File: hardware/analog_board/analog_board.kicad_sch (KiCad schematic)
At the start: 0 parts

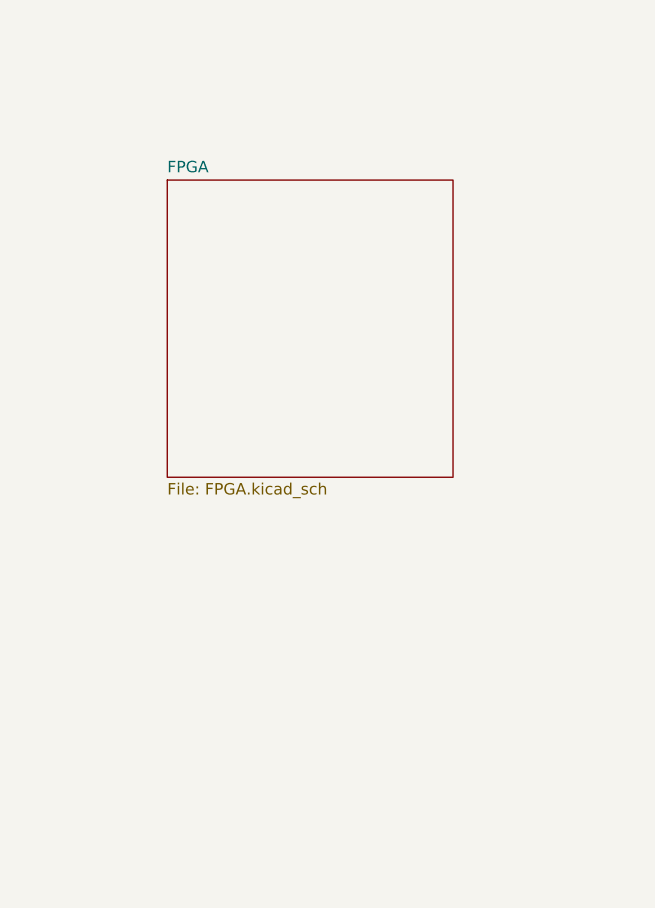
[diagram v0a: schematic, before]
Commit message: 1、FPGA最小系统原理图 2、DAC电路原理图 3、FPGA DAC 预布局
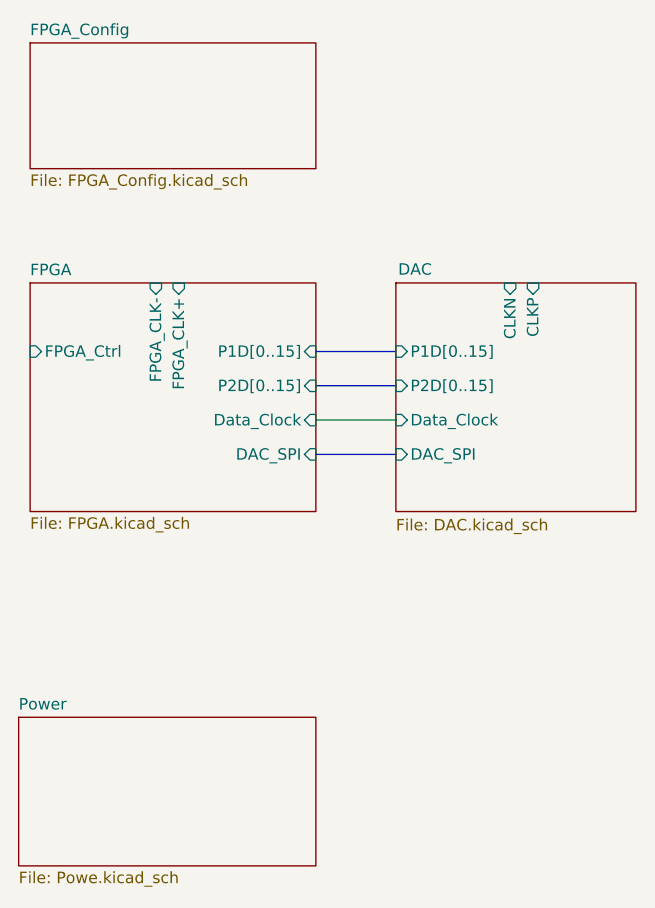
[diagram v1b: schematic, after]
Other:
- added sheet DAC (DAC.kicad_sch)
- added sheet FPGA_Config (FPGA_Config.kicad_sch)
- added sheet Power (Powe.kicad_sch)
- sheet FPGA ports: added DAC_SPI, Data_Clock, FPGA_CLK+, FPGA_CLK-, FPGA_Ctrl, P1D[0..15], P2D[0..15]; removed none

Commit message: feat：时钟电路原理图
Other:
- added sheet Clock (Clock.kicad_sch)
- sheet DAC ports: added DAC_CKL-, DAC_CLK+, OUT1, OUT2; removed CLKN, CLKP
- sheet FPGA ports: added Clock_NRST; removed none

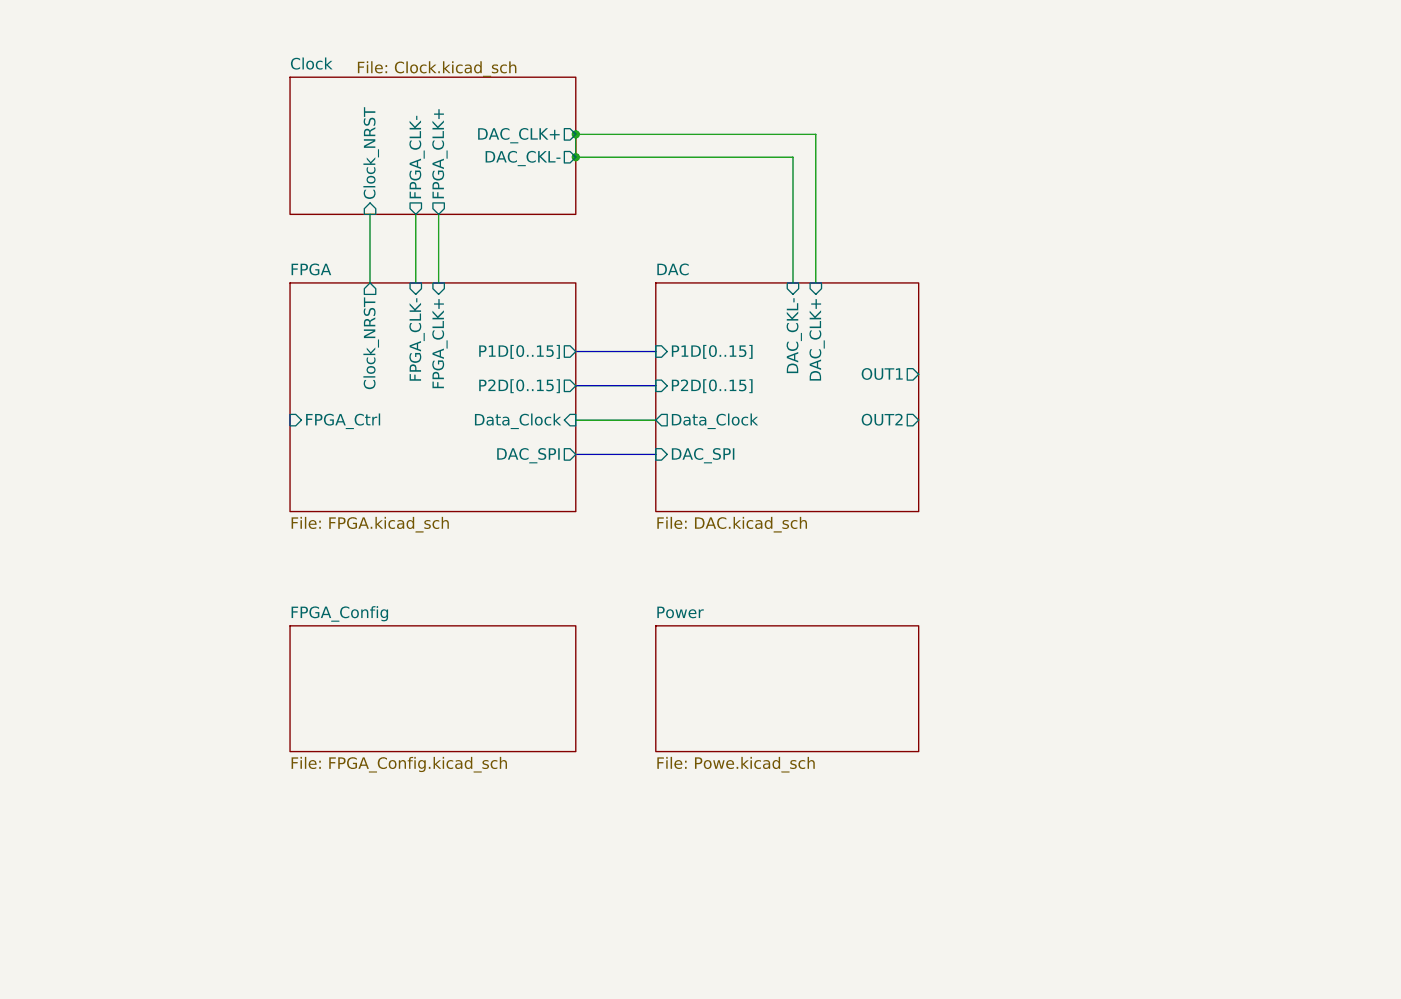
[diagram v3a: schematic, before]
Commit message: feat：完成模拟板板间接口设计
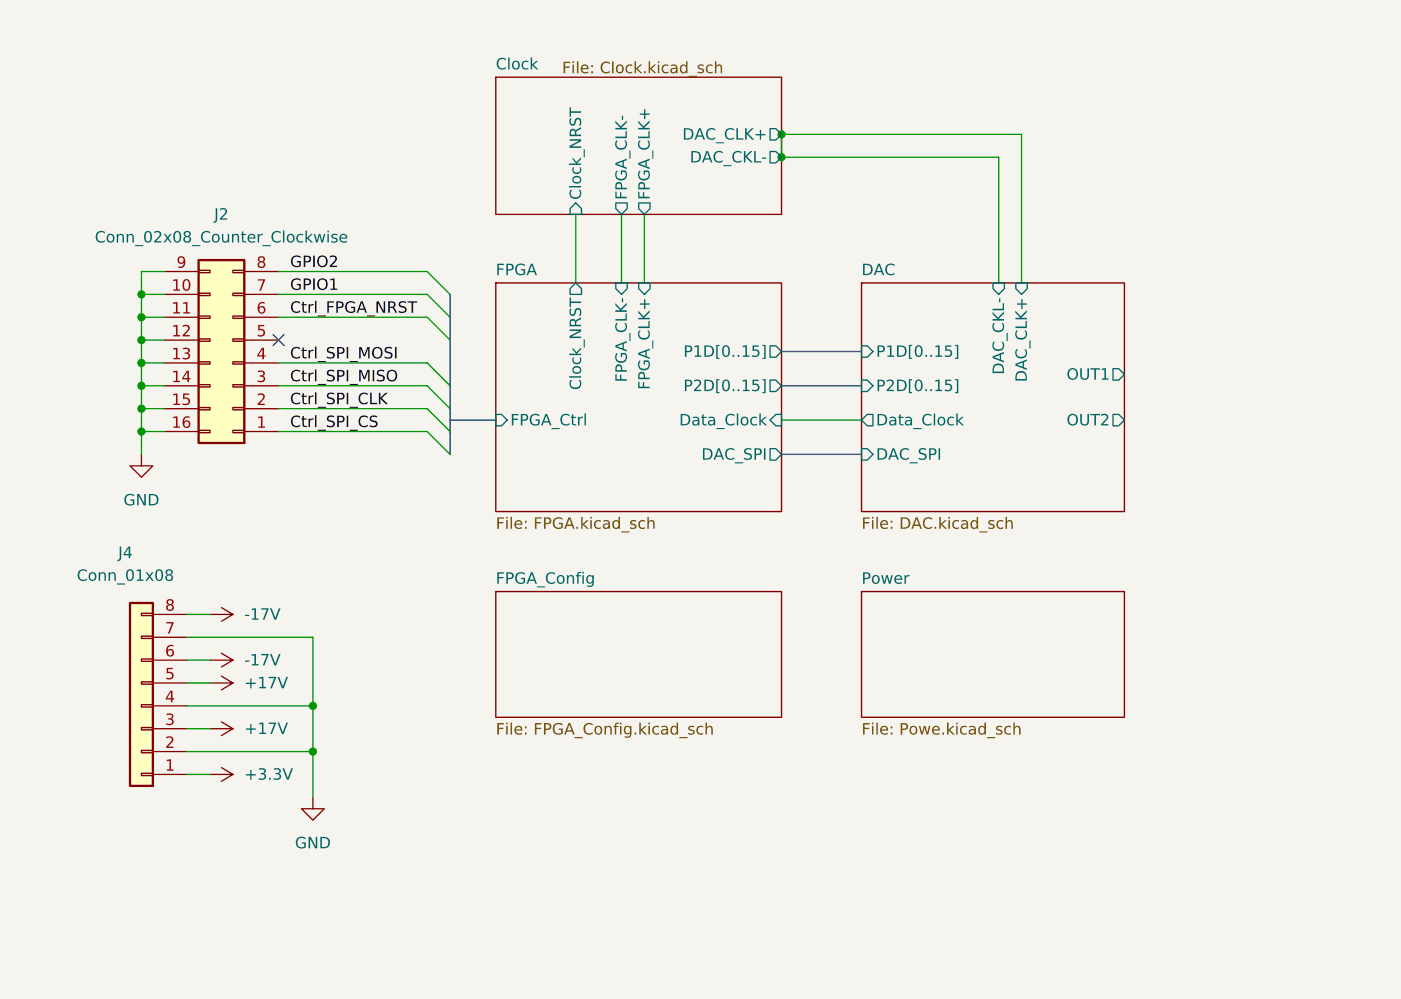
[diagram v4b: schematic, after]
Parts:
- added J2: Conn_02x08_Counter_Clockwise, Connector_IDC:IDC-Header_2x08_P2.54mm_Latch_Vertical, symbol Connector_Generic:Conn_02x08_Counter_Clockwise
- added J4: Conn_01x08, Connector_JST:JST_VH_B8P-VH-B_1x08_P3.96mm_Vertical, symbol Connector_Generic:Conn_01x08
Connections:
- new net +17V: J4.3 (Pin_3), J4.5 (Pin_5)
- new net +3.3V: J4.1 (Pin_1)
- new net -17V: J4.6 (Pin_6), J4.8 (Pin_8)
- new net Ctrl_FPGA_NRST: J2.6 (Pin_6)
- new net Ctrl_SPI_CLK: J2.2 (Pin_2)
- new net Ctrl_SPI_CS: J2.1 (Pin_1)
- new net Ctrl_SPI_MISO: J2.3 (Pin_3)
- new net Ctrl_SPI_MOSI: J2.4 (Pin_4)
- new net GND: J2.10 (Pin_10), J2.11 (Pin_11), J2.12 (Pin_12), J2.13 (Pin_13), J2.14 (Pin_14), J2.15 (Pin_15), J2.16 (Pin_16), J2.9 (Pin_9), J4.2 (Pin_2), J4.4 (Pin_4), J4.7 (Pin_7)
- new net GPIO1: J2.7 (Pin_7)
- new net GPIO2: J2.8 (Pin_8)
- no-connect marks 0 -> 1

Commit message: feat：模拟板电源 原理图设计
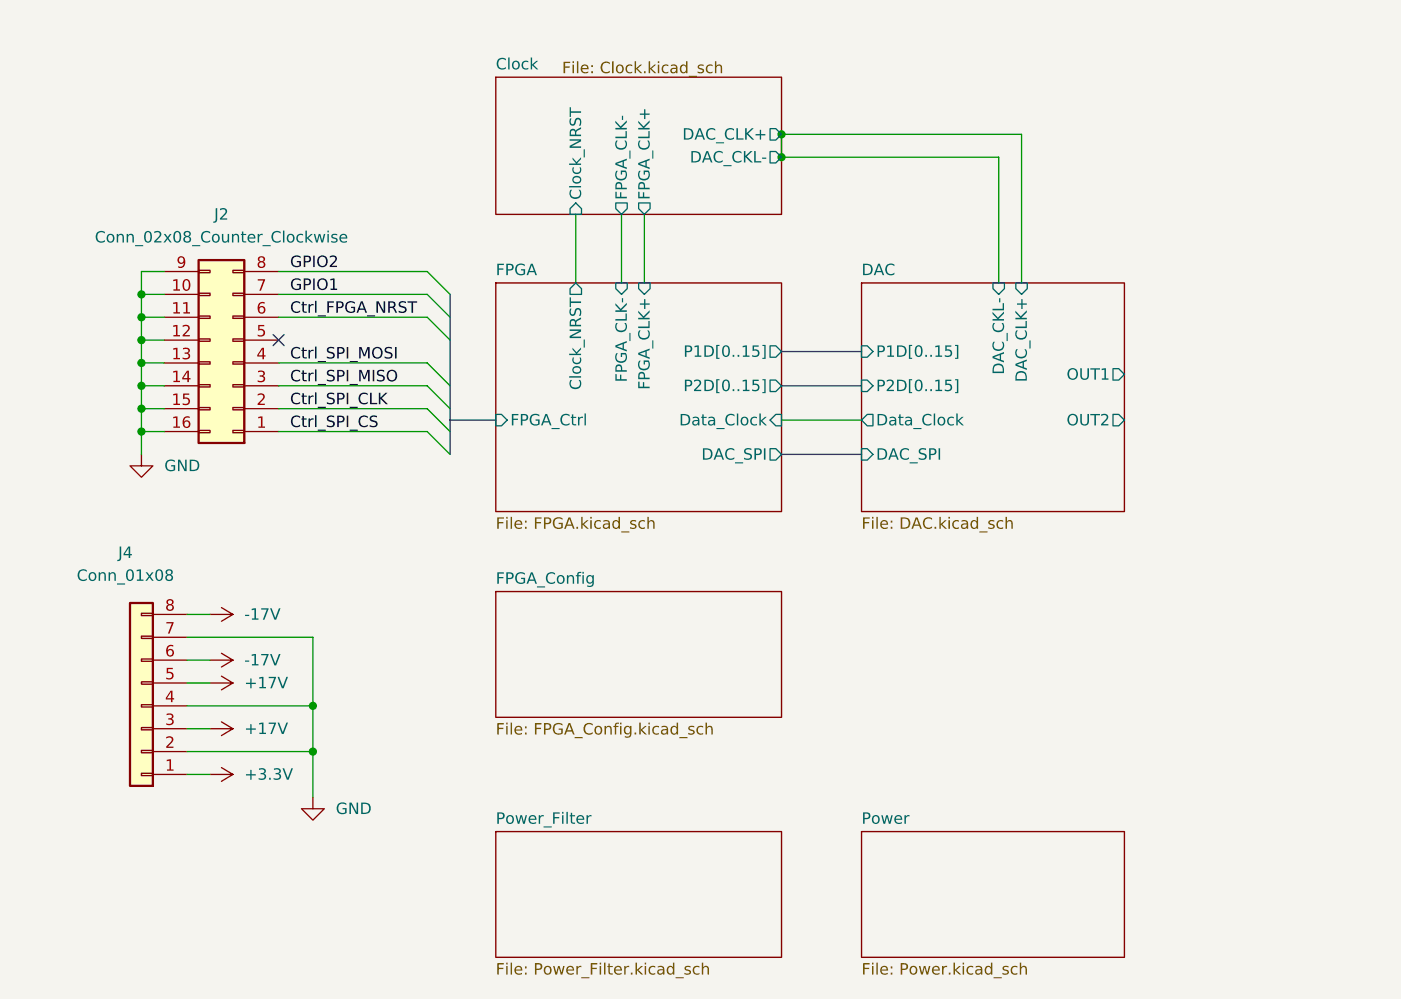
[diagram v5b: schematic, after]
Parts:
- J4: footprint Connector_JST:JST_VH_B8P-VH-B_1x08_P3.96mm_Vertical -> Connector_JST:JST_VH_B8P-VH_1x08_P3.96mm_Vertical
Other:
- added sheet Power_Filter (Power_Filter.kicad_sch)
- sheet Power: file Powe.kicad_sch -> Power.kicad_sch
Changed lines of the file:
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@@
 		)
 		(property "Value" "GND"
-			(at 43.18 129.54 0)
-			(show_name no)
-			(do_not_autoplace no)
-			(effects
-				(font
-					(size 1.27 1.27)
-				)
+			(at 45.72 125.7299 0)
+			(show_name no)
+			(do_not_autoplace no)
+			(effects
+				(font
+					(size 1.27 1.27)
+				)
+				(justify left)
 			)
 		)
@@
 		)
 		(property "Value" "GND"
-			(at 24.13 91.44 0)
-			(show_name no)
-			(do_not_autoplace no)
-			(effects
-				(font
-					(size 1.27 1.27)
-				)
+			(at 26.67 87.6299 0)
+			(show_name no)
+			(do_not_autoplace no)
+			(effects
+				(font
+					(size 1.27 1.27)
+				)
+				(justify left)
 			)
 		)
@@
 			)
 		)
-		(property "Footprint" "Connector_JST:JST_VH_B8P-VH-B_1x08_P3.96mm_Vertical"
+		(property "Footprint" "Connector_JST:JST_VH_B8P-VH_1x08_P3.96mm_Vertical"
 			(at 24.13 114.3 0)
 			(hide yes)
@@
 			(project "analog_board"
 				(path "/ca4be128-f2cd-4bef-b262-ed123f9c630d"
-					(page "5")
+					(page "4")
 				)
 			)
@@
 	)
 	(sheet
-		(at 63.5 44.45)
-		(size 31.75 15.24)
-		(exclude_from_sim no)
-		(in_bom yes)
-		(on_board yes)
-		(dnp no)
-		(stroke
-			(width 0.1524)
-			(type solid)
-		)
-		(fill
-			(color 0 0 0 0)
-		)
-		(property "Sheetname" "Clock"
-			(at 63.5 43.7384 0)
-			(show_name no)
-			(do_not_autoplace no)
-			(effects
-				(font
-					(size 1.27 1.27)
-				)
-				(justify left bottom)
-			)
-		)
-		(property "Sheetfile" "Clock.kicad_sch"
-			(at 70.866 42.672 0)
-			(show_name no)
-			(do_not_autoplace no)
-			(effects
-				(font
-					(size 1.27 1.27)
-				)
-				(justify left top)
-			)
-		)
-		(pin "FPGA_CLK+" output
-			(at 80.01 59.69 270)
-			(effects
-				(font
-					(size 1.27 1.27)
-				)
-				(justify left)
-			)
-		)
-		(pin "FPGA_CLK-" output
-			(at 77.47 59.69 270)
-			(effects
-				(font
-					(size 1.27 1.27)
-				)
-				(justify left)
-			)
-		)
-		(pin "DAC_CLK+" output
-			(at 95.25 50.8 0)
-			(effects
-				(font
-					(size 1.27 1.27)
-				)
-				(justify right)
-			)
-		)
-		(pin "DAC_CKL-" output
-			(at 95.25 53.34 0)
-			(effects
-				(font
-					(size 1.27 1.27)
-				)
-				(justify right)
-			)
-		)
-		(pin "Clock_NRST" input
-			(at 72.39 59.69 270)
-			(effects
-				(font
-					(size 1.27 1.27)
-				)
-				(justify left)
-			)
-		)
-		(instances
-			(project "analog_board"
-				(path "/ca4be128-f2cd-4bef-b262-ed123f9c630d"
-					(page "6")
-				)
-			)
-		)
-	)
-	(sheet
-		(at 104.14 101.6)
+		(at 104.14 128.27)
 		(size 29.21 13.97)
 		(exclude_from_sim no)
@@
 		)
 		(property "Sheetname" "Power"
-			(at 104.14 100.8884 0)
+			(at 104.14 127.5584 0)
 			(show_name no)
 			(do_not_autoplace no)
@@
 			)
 		)
-		(property "Sheetfile" "Powe.kicad_sch"
-			(at 104.14 116.1546 0)
+		(property "Sheetfile" "Power.kicad_sch"
+			(at 104.14 142.8246 0)
 			(show_name no)
 			(do_not_autoplace no)
@@
 			(project "analog_board"
 				(path "/ca4be128-f2cd-4bef-b262-ed123f9c630d"
-					(page "4")
-				)
-			)
+					(page "7")
+				)
+			)
+		)
+	)
+	(sheet
+		(at 63.5 44.45)
+		(size 31.75 15.24)
+		(exclude_from_sim no)
+		(in_bom yes)
+		(on_board yes)
+		(dnp no)
+		(stroke
+			(width 0.1524)
+			(type solid)
+		)
+		(fill
+			(color 0 0 0 0)
+		)
+		(property "Sheetname" "Clock"
+			(at 63.5 43.7384 0)
+			(show_name no)
+			(do_not_autoplace no)
+			(effects
+				(font
+					(size 1.27 1.27)
+				)
+				(justify left bottom)
+			)
+		)
+		(property "Sheetfile" "Clock.kicad_sch"
+			(at 70.866 42.672 0)
+			(show_name no)
+			(do_not_autoplace no)
+			(effects
+				(font
+					(size 1.27 1.27)
+				)
+				(justify left top)
+			)
+		)
+		(pin "FPGA_CLK+" output
+			(at 80.01 59.69 270)
+			(effects
+				(font
+					(size 1.27 1.27)
+				)
+				(justify left)
+			)
+		)
+		(pin "FPGA_CLK-" output
+			(at 77.47 59.69 270)
+			(effects
+				(font
+					(size 1.27 1.27)
+				)
+				(justify left)
+			)
+		)
+		(pin "DAC_CLK+" output
+			(at 95.25 50.8 0)
+			(effects
+				(font
+					(size 1.27 1.27)
+				)
+				(justify right)
+			)
+		)
+		(pin "DAC_CKL-" output
+			(at 95.25 53.34 0)
+			(effects
+				(font
+					(size 1.27 1.27)
+				)
+				(justify right)
+			)
+		)
+		(pin "Clock_NRST" input
+			(at 72.39 59.69 270)
+			(effects
+				(font
+					(size 1.27 1.27)
+				)
+				(justify left)
+			)
+		)
+		(instances
+			(project "analog_board"
+				(path "/ca4be128-f2cd-4bef-b262-ed123f9c630d"
+					(page "5")
+				)
+			)
+		)
+	)
+	(sheet
+		(at 63.5 128.27)
+		(size 31.75 13.97)
+		(exclude_from_sim no)
+		(in_bom yes)
+		(on_board yes)
+		(dnp no)
+		(fields_autoplaced yes)
+		(stroke
+			(width 0.1524)
+			(type solid)
+		)
+		(fill
+			(color 0 0 0 0)
+		)
+		(property "Sheetname" "Power_Filter"
+			(at 63.5 127.5584 0)
+			(show_name no)
+			(do_not_autoplace no)
+			(effects
+				(font
+					(size 1.27 1.27)
+				)
+				(justify left bottom)
+			)
+		)
+		(property "Sheetfile" "Power_Filter.kicad_sch"
+			(at 63.5 142.8246 0)
+			(show_name no)
+			(do_not_autoplace no)
+			(effects
+				(font
+					(size 1.27 1.27)
+				)
+				(justify left top)
+			)
+		)
+		(instances
+			(project "analog_board"
+				(path "/ca4be128-f2cd-4bef-b262-ed123f9c630d"
+					(page "6")
+				)
+			)

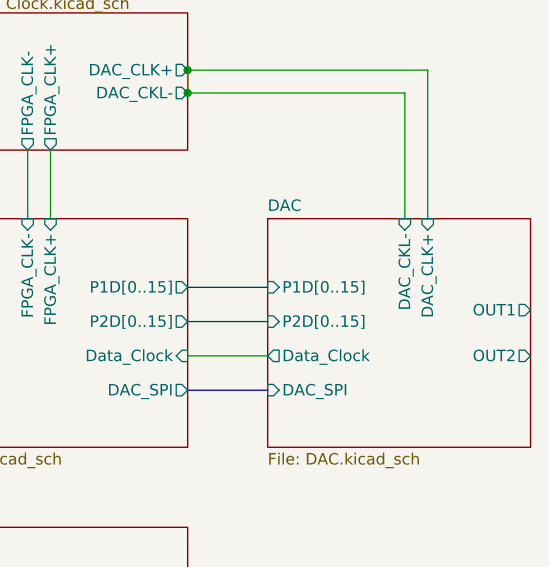
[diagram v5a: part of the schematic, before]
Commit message: feat：时钟电路预布局
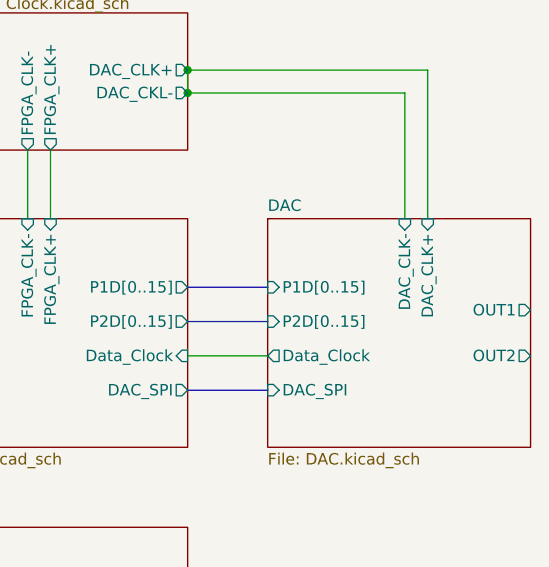
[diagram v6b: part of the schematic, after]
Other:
- sheet DAC ports: added DAC_CLK-; removed DAC_CKL-
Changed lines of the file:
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@@
-			)
-		)
-		(pin "DAC_CKL-" input
-			(at 119.38 67.31 90)
-			(effects
-				(font
-					(size 1.27 1.27)
-				)
-				(justify right)
 			)
 		)
@@
 			(effects
 				(font
+					(size 1.27 1.27)
+				)
+				(justify right)
+			)
+		)
+		(pin "DAC_CLK-" input
+			(at 119.38 67.31 90)
+			(effects
+				(font
